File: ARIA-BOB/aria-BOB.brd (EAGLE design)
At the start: 100 x 80 mm, 15 parts

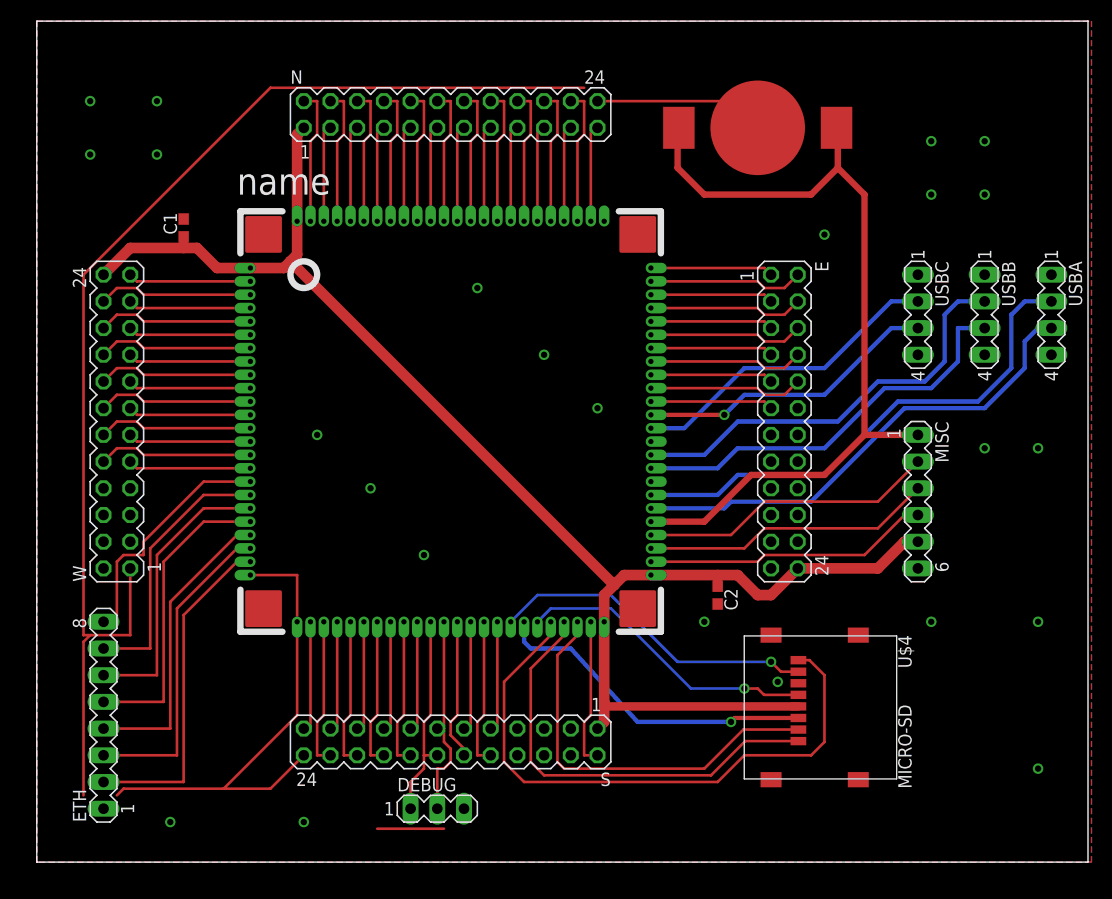
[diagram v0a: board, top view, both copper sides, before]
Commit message: changed board size, increased isolation of gnd
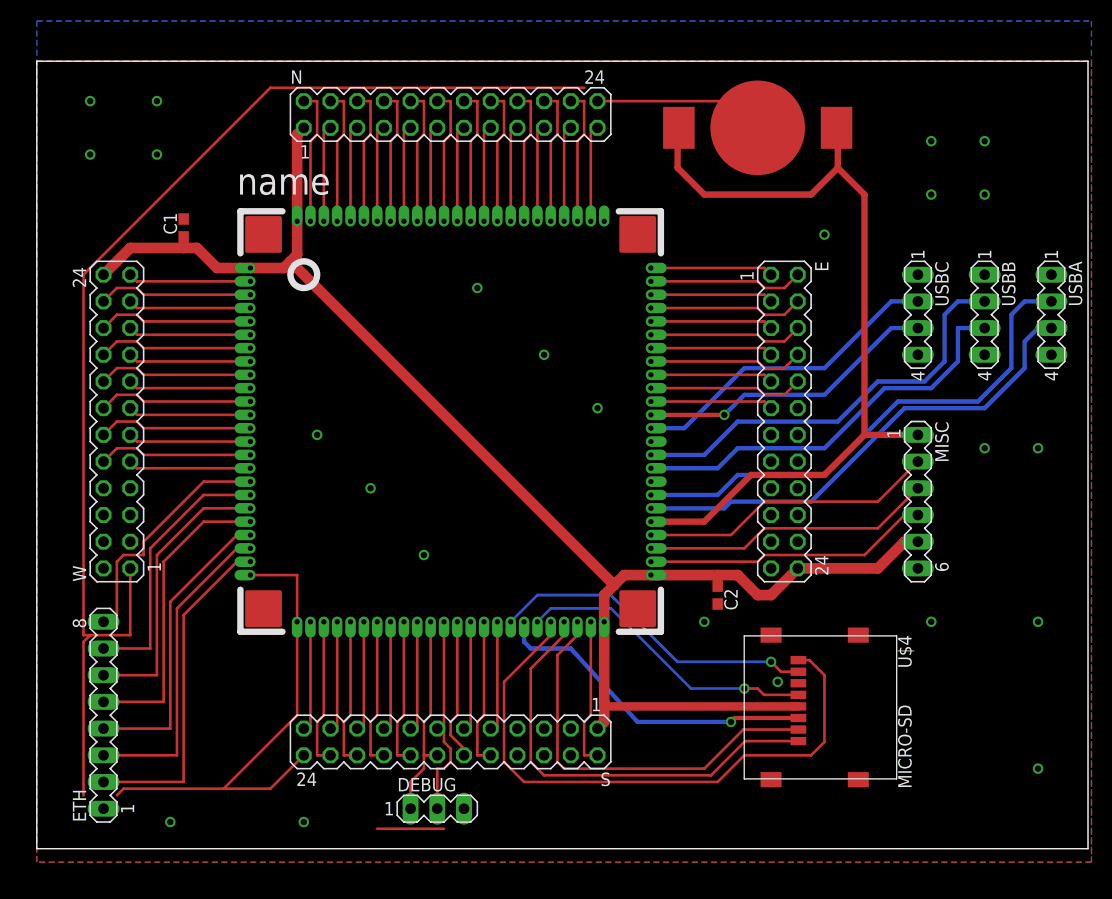
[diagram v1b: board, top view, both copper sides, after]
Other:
- board size 100 x 80 mm -> 100 x 74.9 mm
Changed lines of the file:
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@@
 <setting verticaltext="up"/>
 </settings>
-<grid distance="0.05" unitdist="inch" unit="mm" style="lines" multiple="1" display="no" altdistance="0.025" altunitdist="inch" altunit="inch"/>
+<grid distance="0.05" unitdist="inch" unit="mil" style="lines" multiple="1" display="no" altdistance="0.025" altunitdist="inch" altunit="inch"/>
 <layers>
 <layer number="1" name="Top" color="4" fill="1" visible="yes" active="yes"/>
@@
 <board>
 <plain>
-<wire x1="0" y1="0" x2="100" y2="0" width="0" layer="20"/>
-<wire x1="100" y1="0" x2="100" y2="80" width="0" layer="20"/>
-<wire x1="100" y1="80" x2="0" y2="80" width="0" layer="20"/>
-<wire x1="0" y1="80" x2="0" y2="0" width="0" layer="20"/>
+<wire x1="0" y1="1.27" x2="100" y2="1.27" width="0" layer="20"/>
+<wire x1="100" y1="1.27" x2="100" y2="76.19" width="0" layer="20"/>
+<wire x1="100" y1="76.19" x2="0" y2="76.19" width="0" layer="20"/>
+<wire x1="0" y1="76.19" x2="0" y2="1.27" width="0" layer="20"/>
+<dimension x1="0" y1="1.27" x2="0" y2="76.2" x3="-5.08" y3="38.735" textsize="1.778" layer="20"/>
 </plain>
 <attributes>
@@
 <via x="12.7" y="3.81" extent="1-16" drill="0.6"/>
 <via x="25.4" y="3.81" extent="1-16" drill="0.6"/>
-<polygon width="0.6096" layer="16">
+<polygon width="0.6096" layer="16" isolate="0.4064">
 <vertex x="0" y="80.01"/>
 <vertex x="100.33" y="80.01"/>
@@
 <vertex x="0" y="0"/>
 </polygon>
-<polygon width="0.6096" layer="1">
-<vertex x="0" y="80.01"/>
-<vertex x="100.33" y="80.01"/>
+<polygon width="0.6096" layer="1" isolate="0.4064">
+<vertex x="0" y="76.2"/>
+<vertex x="100.33" y="76.2"/>
 <vertex x="100.33" y="0"/>
 <vertex x="0" y="0"/>
@@
 <contactref element="C1" pad="2"/>
 <contactref element="C2" pad="2"/>
+<wire x1="70.485" y1="17.145" x2="72.45" y2="17.01" width="0" layer="19" extent="1-1"/>
 </signal>
 <signal name="E2">

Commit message: added holes
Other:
- board text added: "Aria Breakout v1"
- board text added: "octanis.org"

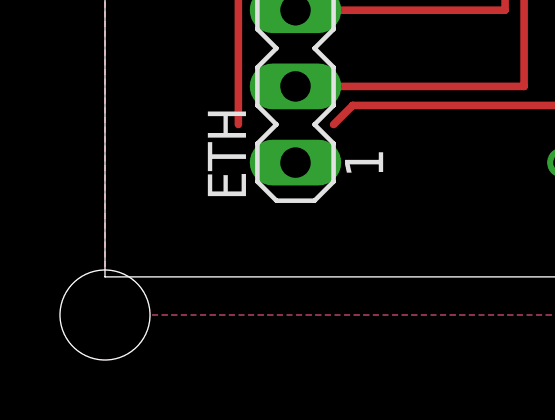
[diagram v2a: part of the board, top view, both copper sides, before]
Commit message: corrected I2C SDA short to 3V
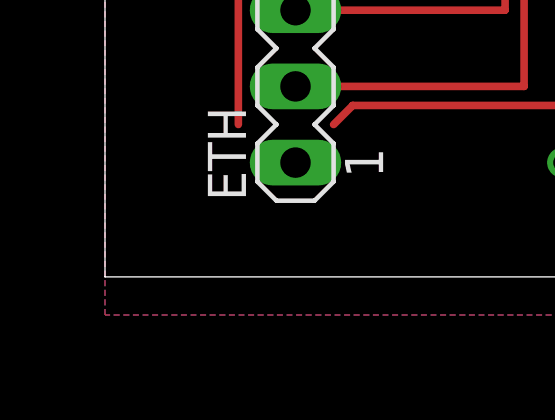
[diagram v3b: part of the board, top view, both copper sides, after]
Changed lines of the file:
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@@
 <wire x1="100" y1="76.19" x2="0" y2="76.19" width="0" layer="20"/>
 <wire x1="0" y1="76.19" x2="0" y2="1.27" width="0" layer="20"/>
-<dimension x1="0" y1="1.27" x2="0" y2="76.2" x3="-5.08" y3="38.735" textsize="1.778" layer="20"/>
 <rectangle x1="90.4621" y1="12.2809" x2="91.3257" y2="12.3063" layer="200"/>
 <rectangle x1="90.2843" y1="12.3063" x2="91.5035" y2="12.3317" layer="200"/>
@@
 <text x="94.6404" y="11.176" size="0.8128" layer="27" font="fixed" rot="R180">octanis.org</text>
 <text x="85.6488" y="20.7264" size="0.8128" layer="27" font="fixed">Aria Breakout v1</text>
-<hole x="0" y="0" drill="3"/>
 <hole x="5.08" y="71.12" drill="3"/>
 <hole x="93.98" y="71.12" drill="3"/>
